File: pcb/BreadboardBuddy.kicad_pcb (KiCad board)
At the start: 4 copper layers, 53 x 25.7 mm, 55 parts, among them J1 Conn_02x02_Odd_Even, J2 Conn_02x02_Odd_Even, J3 Conn_01x08, J4 Conn_01x08, J5 USB_C_Receptacle_USB2.0, J6 Conn_ARM_SWD_TagConnect_TC203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, J7 Conn_01x06, J8 Barrel_Jack_Switch, J9 Conn_02x03_Odd_Even, SW1 SW_SPST, SW2 SW_SPST, SW3 SW_SPST, U1 AP7375-33SA-7, U2 IP4234CZ6,125, U3 W25Q16JVUXIQ TR, U4 RP2040, U5 AP63203WU, Y1 12MHz

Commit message: Prepped for DR
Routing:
- net VBUS: track 60.0 -> 52.3 mm
- net Net-(D1-A): track 0.00 -> 1.41 mm
- net /Microcontroller/RUN: track 40.7 -> 41.3 mm
- net +3V3: track 29.0 -> 29.2 mm, vias 13 -> 12
- added copper zone on B.Cu, net VBUS

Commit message: Prepared for fab
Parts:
- C11: renamed from C3; value 10u -> 22u
- C8: renamed from C11; value 2.2u -> 0.1u
- C9: renamed from C8; value 0.1u -> 2.2u
- J8: renamed from J7; value Conn_01x06 -> Conn_01x05
- renumbered C13 to C1, C15 to C10, C5 to C12, C9 to C13, C16 to C14, C17 to C15, C19 to C16, C18 to C17, C1 to C18, C2 to C19, C10 to C2, C12 to C3, C7 to C4, C14 to C5, C4 to C6, C6 to C7, D5 to D1, D4 to D2, D1 to D4, D2 to D5, F2 to F1, F1 to F2, J8 to J1, J5 to J2, J1 to J3, J2 to J4, J9 to J5, J3 to J6, J4 to J7, J6 to J9, R8 to R1, R6 to R2, R10 to R3, R9 to R4, R1 to R5, R2 to R6, R4 to R7, R5 to R8, R3 to R9, SW2 to SW1, SW1 to SW2, U4 to U1, U3 to U2, U5 to U3, U1 to U4, U2 to U5
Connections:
- net /Connectors/CC1 renamed /CC1
- net /Connectors/CC2 renamed /CC2
- net /Connectors/USB_D+_RAW renamed /USB_D+_RAW
- net /Connectors/USB_D-_RAW renamed /USB_D-_RAW
- net /Connectors/USB_SHLD renamed /USB_SHLD
- R1 pad 2: Net-(U4-GPIO16) -> Net-(U1-GPIO25)
- U1 pad 27: Net-(U4-GPIO16) -> unconnected-(U1-GPIO16-Pad27)
- U1 pad 37: unconnected-(U4-GPIO25-Pad37) -> Net-(U1-GPIO25)
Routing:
- net Net-(U1-GPIO25): track 0.00 -> 7.58 mm, vias 0 -> 2
- net +3V3: track 29.2 -> 35.6 mm, vias 12 -> 20
- net Net-(U4-GPIO16): track 2.29 -> 0.00 mm
- net GND: track 22.5 -> 24.0 mm, vias 28 -> 43
- net +1V1: track 25.7 -> 26.8 mm, vias 3 -> 6
- net VUSB: track 54.4 -> 55.0 mm
- added copper zone on F.Cu, net +3V3
- added copper zone on In2.Cu, net GND
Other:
- outline, holes or cut-outs redrawn
- board text added: "${REVISION} ${ISSUE_DATE}"
- board text added: "5-30V"

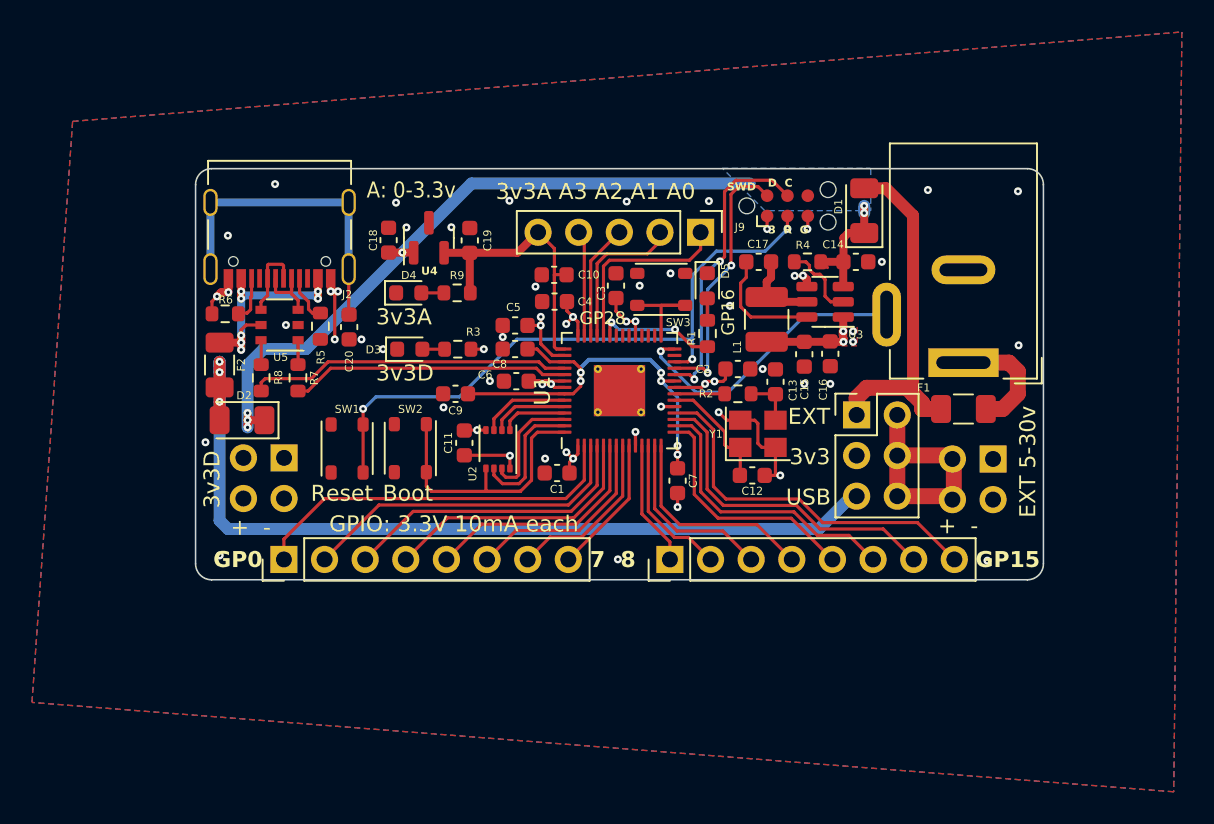
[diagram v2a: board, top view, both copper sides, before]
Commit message: Fixed board USB issue
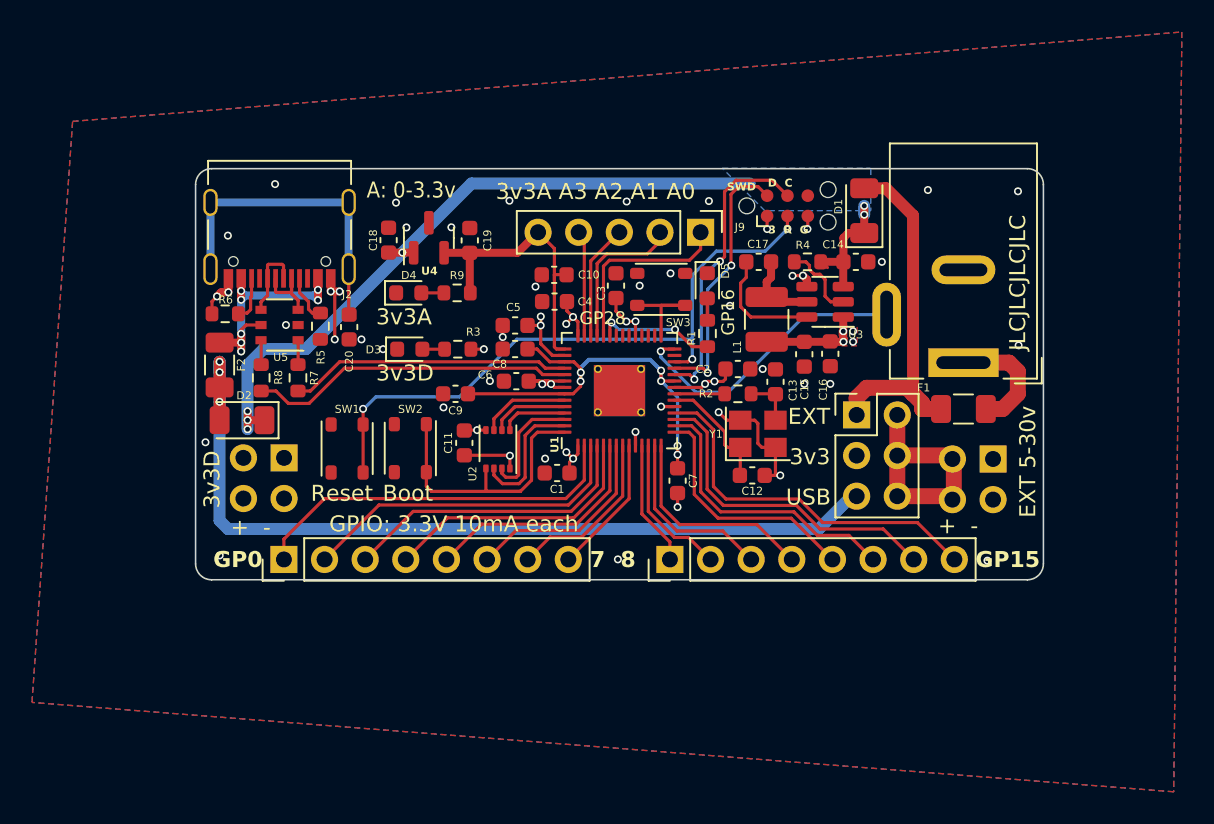
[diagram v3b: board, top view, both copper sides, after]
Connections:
- J2 pad A6: /USB_D-_RAW -> /USB_D+_RAW
- J2 pad A7: /USB_D+_RAW -> /USB_D-_RAW
- J2 pad B6: /USB_D-_RAW -> /USB_D+_RAW
- J2 pad B7: /USB_D+_RAW -> /USB_D-_RAW
- R7 pad 2: USB_D+ -> USB_D-
- R8 pad 2: USB_D- -> USB_D+
- U5 pad 3: /USB_D+_RAW -> /USB_D-_RAW
- U5 pad 4: /USB_D-_RAW -> /USB_D+_RAW
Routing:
- net USB_D+: track 17.5 -> 20.4 mm
- net USB_D-: track 20.4 -> 17.8 mm
- net VBUS_RAW: track 16.2 -> 16.9 mm
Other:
- board text added: "JLCJLCJLCJLC"

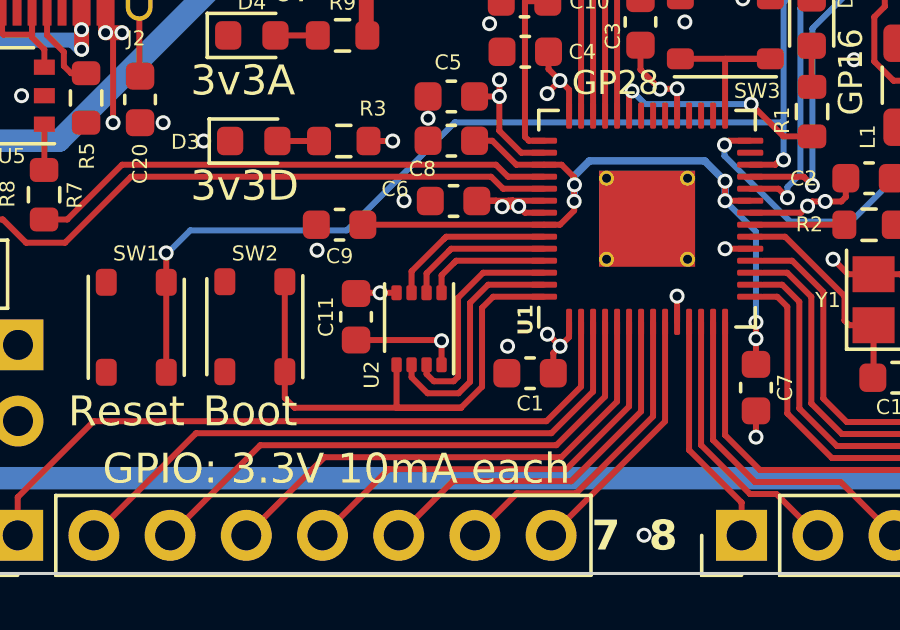
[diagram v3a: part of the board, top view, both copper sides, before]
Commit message: Improved flash footprint
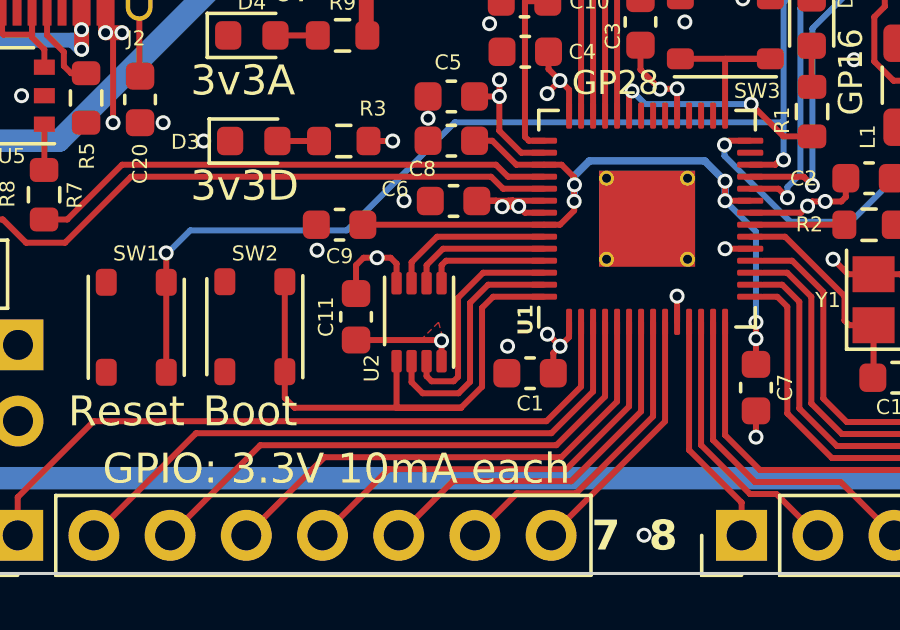
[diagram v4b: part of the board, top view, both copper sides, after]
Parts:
- moved U2 0.22 mm to (125.9, 110.5)
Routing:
- net +3V3: track 35.6 -> 37.4 mm
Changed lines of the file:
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@@
 	(footprint "BreadboardBuddy:8-UFDFN"
 		(layer "F.Cu")
-		(at 125.899584 110.669045 90)
+		(at 125.899584 110.45 90)
 		(property "Reference" "U2"
 			(at -1.530955 -1.579584 90)
@@
 			)
 		)
-		(sheetname "Microcontroller")
-		(sheetfile "microcontroller.kicad_sch")
 		(attr smd)
 		(fp_line
@@
 			(layer "F.SilkS")
 		)
-		(fp_poly
-			(pts
-				(xy -1.749999 -1.25) (xy 1.749999 -1.25) (xy 1.749999 1.25) (xy -1.749999 1.25)
-			)
+		(fp_rect
+			(start -1.75 -1.25)
+			(end 1.75 1.25)
 			(stroke
 				(width 0.05)
@@
 		)
 		(pad "1" smd roundrect
-			(at -1.2 -0.75 90)
-			(size 0.5 0.35)
+			(at -1.3 -0.75 90)
+			(size 0.75 0.35)
 			(layers "F.Cu" "F.Paste" "F.Mask")
 			(roundrect_rratio 0.2)
@@
 		)
 		(pad "2" smd roundrect
-			(at -1.2 -0.25 90)
-			(size 0.5 0.35)
+			(at -1.3 -0.25 90)
+			(size 0.75 0.35)
 			(layers "F.Cu" "F.Paste" "F.Mask")
 			(roundrect_rratio 0.2)
@@
 		)
 		(pad "3" smd roundrect
-			(at -1.2 0.25 90)
-			(size 0.5 0.35)
+			(at -1.3 0.25 90)
+			(size 0.75 0.35)
 			(layers "F.Cu" "F.Paste" "F.Mask")
 			(roundrect_rratio 0.2)
@@
 		)
 		(pad "4" smd roundrect
-			(at -1.2 0.75 90)
-			(size 0.5 0.35)
+			(at -1.3 0.75 90)
+			(size 0.75 0.35)
 			(layers "F.Cu" "F.Paste" "F.Mask")
 			(roundrect_rratio 0.2)
@@
 		)
 		(pad "5" smd roundrect
-			(at 1.2 0.75 90)
-			(size 0.5 0.35)
+			(at 1.3 0.75 90)
+			(size 0.75 0.35)
 			(layers "F.Cu" "F.Paste" "F.Mask")
 			(roundrect_rratio 0.2)
@@
 		)
 		(pad "6" smd roundrect
-			(at 1.2 0.25 90)
-			(size 0.5 0.35)
+			(at 1.3 0.25 90)
+			(size 0.75 0.35)
 			(layers "F.Cu" "F.Paste" "F.Mask")
 			(roundrect_rratio 0.2)
@@
 		)
 		(pad "7" smd roundrect
-			(at 1.2 -0.25 90)
-			(size 0.5 0.35)
+			(at 1.3 -0.25 90)
+			(size 0.75 0.35)
 			(layers "F.Cu" "F.Paste" "F.Mask")
 			(roundrect_rratio 0.2)
@@
 		)
 		(pad "8" smd roundrect
-			(at 1.2 -0.75 90)
-			(size 0.5 0.35)
+			(at 1.3 -0.75 90)
+			(size 0.75 0.35)
 			(layers "F.Cu" "F.Paste" "F.Mask")
 			(roundrect_rratio 0.2)
@@
 	)
 	(segment
-		(start 123.824584 109.469045)
-		(end 123.799584 109.494045)
+		(start 125.149584 108.499584)
+		(end 125.149584 109.15)
 		(width 0.2)
 		(layer "F.Cu")
@@
 	)
 	(segment
+		(start 124.5 108.3)
+		(end 124.05 108.3)
+		(width 0.2)
+		(layer "F.Cu")
+		(net 4)
+	)
+	(segment
 		(start 125.02 104.41)
 		(end 124.215 104.41)
@@
 	)
 	(segment
-		(start 124.599584 109.469045)
-		(end 123.824584 109.469045)
+		(start 124.05 108.3)
+		(end 123.799584 108.550416)
 		(width 0.2)
 		(layer "F.Cu")
@@
 	)
 	(segment
+		(start 124.95 108.3)
+		(end 125.149584 108.499584)
+		(width 0.2)
+		(layer "F.Cu")
+		(net 4)
+	)
+	(segment
 		(start 129.22 106.59)
 		(end 129.43 106.8)
@@
 	)
 	(segment
+		(start 123.799584 108.550416)
+		(end 123.799584 109.494045)
+		(width 0.2)
+		(layer "F.Cu")
+		(net 4)
+	)
+	(segment
 		(start 130.2 110.85)
 		(end 130.6 111.25)
@@
 	)
 	(segment
-		(start 125.149584 109.469045)
-		(end 124.599584 109.469045)
-		(width 0.2)
-		(layer "F.Cu")
-		(net 4)
-	)
-	(segment
 		(start 147.4875 103.29)
 		(end 147.4875 103.7375)
@@
 	)
 	(segment
+		(start 124.5 108.3)
+		(end 124.95 108.3)
+		(width 0.2)
+		(layer "F.Cu")
+		(net 4)
+	)
+	(segment
 		(start 129.03 106.4)
 		(end 128.95 106.4)
@@
 	)
 	(via
-		(at 124.599584 109.469045)
+		(at 124.5 108.3)
 		(size 0.5)
 		(drill 0.3)
@@
 	)
 	(segment
-		(start 128.037257 108.8)
-		(end 130.0625 108.8)
+		(start 126.149584 111.869045)
+		(end 126.149584 112.249584)
 		(width 0.2)
 		(layer "F.Cu")
@@
 	)
 	(segment
-		(start 127.199584 112.269045)
-		(end 127.199584 109.637674)
+		(start 127.049584 112.419045)
+		(end 127.199584 112.269045)
 		(width 0.2)
 		(layer "F.Cu")
@@
 	)
 	(segment
-		(start 126.389384 112.419045)
-		(end 127.049584 112.419045)
+		(start 126.149584 112.249584)
+		(end 126.319045 112.419045)
 		(width 0.2)
 		(layer "F.Cu")
@@
 	)
 	(segment
-		(start 126.149584 111.869045)
-		(end 126.149584 112.179245)
+		(start 127.199584 109.637674)
+		(end 128.037257 108.8)
 		(width 0.2)
 		(layer "F.Cu")
@@
 	)
 	(segment
-		(start 126.149584 112.179245)
-		(end 126.389384 112.419045)
+		(start 126.319045 112.419045)
+		(end 127.049584 112.419045)
 		(width 0.2)
 		(layer "F.Cu")
@@
 	)
 	(segment
-		(start 127.199584 109.637674)
-		(end 128.037257 108.8)
+		(start 127.199584 112.269045)
+		(end 127.199584 109.637674)
 		(width 0.2)
 		(layer "F.Cu")
@@
 	)
 	(segment
-		(start 127.049584 112.419045)
-		(end 127.199584 112.269045)
+		(start 128.037257 108.8)
+		(end 130.0625 108.8)
 		(width 0.2)
 		(layer "F.Cu")
@@
 	)
 	(segment
-		(start 126.183898 112.819045)
-		(end 125.649584 112.284731)
+		(start 128.202944 109.199999)
+		(end 127.599584 109.803359)
 		(width 0.2)
 		(layer "F.Cu")
@@
 	)
 	(segment
-		(start 130.0625 109.199999)
-		(end 128.202944 109.199999)
+		(start 126.019045 112.819045)
+		(end 125.649584 112.449584)
 		(width 0.2)
 		(layer "F.Cu")
@@
 	)
 	(segment
-		(start 127.599584 112.434731)
-		(end 127.215269 112.819045)
+		(start 127.215269 112.819045)
+		(end 126.019045 112.819045)
 		(width 0.2)
 		(layer "F.Cu")
@@
 	)
 	(segment
-		(start 125.649584 112.284731)
+		(start 125.649584 112.449584)
 		(end 125.649584 111.869045)
 		(width 0.2)
@@
 	)
 	(segment
-		(start 128.202944 109.199999)
-		(end 127.599584 109.803359)
+		(start 127.599584 112.434731)
+		(end 127.215269 112.819045)
 		(width 0.2)
 		(layer "F.Cu")
@@
 	)
 	(segment
-		(start 127.215269 112.819045)
-		(end 126.183898 112.819045)
+		(start 130.0625 109.199999)
+		(end 128.202944 109.199999)
 		(width 0.2)
 		(layer "F.Cu")
@@
 	)
 	(segment
-		(start 127.065271 108.469045)
-		(end 127.134316 108.4)
-		(width 0.2)
-		(layer "F.Cu")
-		(net 27)
-	)
-	(segment
-		(start 126.649584 108.884732)
-		(end 127.065271 108.469045)
+		(start 126.649584 109.15)
+		(end 126.649584 108.550416)
 		(width 0.2)
 		(layer "F.Cu")
@@
 	)
 	(segment
-		(start 127.134316 108.4)
+		(start 126.8 108.4)
 		(end 130.0625 108.4)
 		(width 0.2)
@@
 	)
 	(segment
-		(start 126.649584 109.469045)
-		(end 126.649584 108.884732)
+		(start 126.649584 108.550416)
+		(end 126.8 108.4)
 		(width 0.2)
 		(layer "F.Cu")
@@
 	)
 	(segment
-		(start 125.649584 109.469045)
-		(end 125.649584 108.75336)
-		(width 0.2)
-		(layer "F.Cu")
-		(net 29)
-	)
-	(segment
-		(start 125.649584 108.75336)
-		(end 126.733899 107.669045)
+		(start 126.499999 107.600001)
+		(end 130.0625 107.600001)
 		(width 0.2)
 		(layer "F.Cu")
@@
 	)
 	(segment
-		(start 126.802943 107.600001)
-		(end 130.0625 107.600001)
+		(start 125.649584 109.15)
+		(end 125.649584 108.450416)
 		(width 0.2)
 		(layer "F.Cu")
@@
 	)
 	(segment
-		(start 126.733899 107.669045)
-		(end 126.802943 107.600001)
+		(start 125.649584 108.450416)
+		(end 126.499999 107.600001)
 		(width 0.2)
 		(layer "F.Cu")
@@
 	)
 	(segment
-		(start 126.96863 108)
-		(end 130.0625 108)
+		(start 126.149584 109.15)
+		(end 126.149584 108.550416)
 		(width 0.2)
 		(layer "F.Cu")
@@
 	)
 	(segment
-		(start 126.899585 108.069045)
-		(end 126.96863 108)
-		(width 0.2)
-		(layer "F.Cu")
-		(net 31)
-	)
-	(segment
-		(start 126.149584 109.469045)
-		(end 126.149584 108.819046)
+		(start 126.7 108)
+		(end 130.0625 108)
 		(width 0.2)
 		(layer "F.Cu")
@@
 	)
 	(segment
-		(start 126.149584 108.819046)
-		(end 126.899585 108.069045)
+		(start 126.149584 108.550416)
+		(end 126.7 108)
 		(width 0.2)
 		(layer "F.Cu")
@@
 	)
 	(zone
+		(net 2)
+		(net_name "GND")
+		(layer "F.Cu")
+		(hatch edge 0.5)
+		(priority 4)
+		(connect_pads yes
+			(clearance 0.2)
+		)
+		(min_thickness 0.25)
+		(filled_areas_thickness no)
+		(fill yes
+			(thermal_gap 0.5)
+			(thermal_bridge_width 0.5)
+		)
+		(polygon
+			(pts
+				(xy 125.95 111.05) (xy 126.55 110.45) (xy 126.7 111)
+			)
+		)
+	)
+	(zone
